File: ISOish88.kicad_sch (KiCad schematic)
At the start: 285 parts, among them J1 Conn_01x04_Pin, J3 USB_C_Receptacle_USB2.0_14P, K1 Esc, K10 F9, K11 F10, K12 F11, K13 F12, K14 Print, K15 Scroll, K16 Pause, K17 ` ~, K18 1, K19 2, K2 F1, K20 3, K21 4, K22 5, K23 6, K24 7, K25 8, K26 9, K27 0, K28 - _, K29 = +, K3 F2, K30 Backspace, K31 Ins, K32 Home, K33 PgUp, K34 Tab, K35 Q, K36 W, K37 E, K38 R, K39 T, K4 F3, K40 Y, K41 U, K42 I, K43 O, K44 P, K45 [ {, K46 ] }, K47 Enter, K48 Del, K49 End, K5 F4, K50 PgDn, K51 Caps, K52 A, K53 S, K54 D, K55 F, K56 G, K57 H, K58 J, K59 K, K6 F5, K60 L, K61 ; :, K62 ' ", K63 \ |, K64 LShift, K65 Z, K66 X, K67 C, K68 V, K69 B, K7 F6, K70 N, K71 M, K72 , <, K73 . >, K74 / ?, K75 SplitRShift, K76 Fn, K77 Up, K78 LCtrl, K79 LSys, K8 F7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

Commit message: initial f13 revision
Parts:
- added D47: 1N4148W, Diode_SMD:D_SOD-123, symbol Diode:1N4148W
- added K91: F13, Switch_Keyboard_Hotswap_Kailh_mine:SW_Hotswap_Kailh_MX_1.00u, symbol keyboard_parts:KEYSW
- added LD89: SK6812MINI-E, schizobovine:LED_SK6812MINI_PLCC4_3.1x2.7mm_P1.75mm_reverse_mount, symbol schizobovine:SK6812MINI
- BD1, BD10, BD11, BD12, BD13, BD14, BD15, BD16, BD2, BD3, BD4, BD5, BD6, BD7, BD8, BD9: footprint schizobovine:LED_WS2812B_NANO_2020 -> LED_SMD:LED_SK6812MINI_PLCC4_3.5x3.5mm_P1.75mm; symbol schizobovine:WS2812B -> schizobovine:SK6812MINI
- LD1, LD10, LD11, LD12, LD13, LD14, LD15, LD16, LD17, LD18, LD19, LD2, LD20, LD21, LD22, LD23, LD24, LD25, LD26, LD27, LD28, LD29, LD3, LD30, LD31, LD32, LD33, LD34, LD35, LD36, LD37, LD38, LD39, LD4, LD40, LD41, LD42, LD43, LD44, LD45, LD46, LD47, LD48, LD49, LD5, LD50, LD51, LD52, LD53, LD54, LD55, LD56, LD57, LD58, LD59, LD6, LD60, LD61, LD62, LD63, LD64, LD65, LD66, LD67, LD68, LD69, LD7, LD70, LD71, LD72, LD73, LD74, LD75, LD76, LD77, LD78, LD79, LD8, LD80, LD81, LD82, LD83, LD84, LD85, LD86, LD87, LD88, LD9: value WS2812B -> SK6812MINI-E; symbol schizobovine:WS2812B -> schizobovine:SK6812MINI
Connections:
- net +5V: now also BD1.1 (VDD), BD10.1 (VDD), BD11.1 (VDD), BD12.1 (VDD), BD13.1 (VDD), BD14.1 (VDD), BD15.1 (VDD), BD16.1 (VDD), BD2.1 (VDD), BD3.1 (VDD), BD4.1 (VDD), BD5.1 (VDD), BD6.1 (VDD), BD7.1 (VDD), BD8.1 (VDD), BD9.1 (VDD), LD1.1 (VDD), LD10.1 (VDD), LD11.1 (VDD), LD12.1 (VDD), LD13.1 (VDD), LD14.1 (VDD), LD15.1 (VDD), LD16.1 (VDD), LD17.1 (VDD), LD18.1 (VDD), LD19.1 (VDD), LD2.1 (VDD), LD20.1 (VDD), LD21.1 (VDD), LD22.1 (VDD), LD23.1 (VDD), LD24.1 (VDD), LD25.1 (VDD), LD26.1 (VDD), LD27.1 (VDD), LD28.1 (VDD), LD29.1 (VDD), LD3.1 (VDD), LD30.1 (VDD), LD31.1 (VDD), LD32.1 (VDD), LD33.1 (VDD), LD34.1 (VDD), LD35.1 (VDD), LD36.1 (VDD), LD37.1 (VDD), LD38.1 (VDD), LD39.1 (VDD), LD4.1 (VDD), LD40.1 (VDD), LD41.1 (VDD), LD42.1 (VDD), LD43.1 (VDD), LD44.1 (VDD), LD45.1 (VDD), LD46.1 (VDD), LD47.1 (VDD), LD48.1 (VDD), LD49.1 (VDD), LD5.1 (VDD), LD50.1 (VDD), LD51.1 (VDD), LD52.1 (VDD), LD53.1 (VDD), LD54.1 (VDD), LD55.1 (VDD), LD56.1 (VDD), LD57.1 (VDD), LD58.1 (VDD), LD59.1 (VDD), LD6.1 (VDD), LD60.1 (VDD), LD61.1 (VDD), LD62.1 (VDD), LD63.1 (VDD), LD64.1 (VDD), LD65.1 (VDD), LD66.1 (VDD), LD67.1 (VDD), LD68.1 (VDD), LD69.1 (VDD), LD7.1 (VDD), LD70.1 (VDD), LD71.1 (VDD), LD72.1 (VDD), LD73.1 (VDD), LD74.1 (VDD), LD75.1 (VDD), LD76.1 (VDD), LD77.1 (VDD), LD78.1 (VDD), LD79.1 (VDD), LD8.1 (VDD), LD80.1 (VDD), LD81.1 (VDD), LD82.1 (VDD), LD83.1 (VDD), LD84.1 (VDD), LD85.1 (VDD), LD86.1 (VDD), LD87.1 (VDD), LD88.1 (VDD), LD9.1 (VDD), LD89.1 (VDD); no longer BD1.4 (VDD), BD10.4 (VDD), BD11.4 (VDD), BD12.4 (VDD), BD13.4 (VDD), BD14.4 (VDD), BD15.4 (VDD), BD16.4 (VDD), BD2.4 (VDD), BD3.4 (VDD), BD4.4 (VDD), BD5.4 (VDD), BD6.4 (VDD), BD7.4 (VDD), BD8.4 (VDD), BD9.4 (VDD), LD1.4 (VDD), LD10.4 (VDD), LD11.4 (VDD), LD12.4 (VDD), LD13.4 (VDD), LD14.4 (VDD), LD15.4 (VDD), LD16.4 (VDD), LD17.4 (VDD), LD18.4 (VDD), LD19.4 (VDD), LD2.4 (VDD), LD20.4 (VDD), LD21.4 (VDD), LD22.4 (VDD), LD23.4 (VDD), LD24.4 (VDD), LD25.4 (VDD), LD26.4 (VDD), LD27.4 (VDD), LD28.4 (VDD), LD29.4 (VDD), LD3.4 (VDD), LD30.4 (VDD), LD31.4 (VDD), LD32.4 (VDD), LD33.4 (VDD), LD34.4 (VDD), LD35.4 (VDD), LD36.4 (VDD), LD37.4 (VDD), LD38.4 (VDD), LD39.4 (VDD), LD4.4 (VDD), LD40.4 (VDD), LD41.4 (VDD), LD42.4 (VDD), LD43.4 (VDD), LD44.4 (VDD), LD45.4 (VDD), LD46.4 (VDD), LD47.4 (VDD), LD48.4 (VDD), LD49.4 (VDD), LD5.4 (VDD), LD50.4 (VDD), LD51.4 (VDD), LD52.4 (VDD), LD53.4 (VDD), LD54.4 (VDD), LD55.4 (VDD), LD56.4 (VDD), LD57.4 (VDD), LD58.4 (VDD), LD59.4 (VDD), LD6.4 (VDD), LD60.4 (VDD), LD61.4 (VDD), LD62.4 (VDD), LD63.4 (VDD), LD64.4 (VDD), LD65.4 (VDD), LD66.4 (VDD), LD67.4 (VDD), LD68.4 (VDD), LD69.4 (VDD), LD7.4 (VDD), LD70.4 (VDD), LD71.4 (VDD), LD72.4 (VDD), LD73.4 (VDD), LD74.4 (VDD), LD75.4 (VDD), LD76.4 (VDD), LD77.4 (VDD), LD78.4 (VDD), LD79.4 (VDD), LD8.4 (VDD), LD80.4 (VDD), LD81.4 (VDD), LD82.4 (VDD), LD83.4 (VDD), LD84.4 (VDD), LD85.4 (VDD), LD86.4 (VDD), LD87.4 (VDD), LD88.4 (VDD), LD9.4 (VDD)
- net GND: now also BD1.3 (VSS), BD10.3 (VSS), BD11.3 (VSS), BD12.3 (VSS), BD13.3 (VSS), BD14.3 (VSS), BD15.3 (VSS), BD16.3 (VSS), BD2.3 (VSS), BD3.3 (VSS), BD4.3 (VSS), BD5.3 (VSS), BD6.3 (VSS), BD7.3 (VSS), BD8.3 (VSS), BD9.3 (VSS), LD1.3 (VSS), LD10.3 (VSS), LD11.3 (VSS), LD12.3 (VSS), LD13.3 (VSS), LD14.3 (VSS), LD15.3 (VSS), LD16.3 (VSS), LD17.3 (VSS), LD18.3 (VSS), LD19.3 (VSS), LD2.3 (VSS), LD20.3 (VSS), LD21.3 (VSS), LD22.3 (VSS), LD23.3 (VSS), LD24.3 (VSS), LD25.3 (VSS), LD26.3 (VSS), LD27.3 (VSS), LD28.3 (VSS), LD29.3 (VSS), LD3.3 (VSS), LD30.3 (VSS), LD31.3 (VSS), LD32.3 (VSS), LD33.3 (VSS), LD34.3 (VSS), LD35.3 (VSS), LD36.3 (VSS), LD37.3 (VSS), LD38.3 (VSS), LD39.3 (VSS), LD4.3 (VSS), LD40.3 (VSS), LD41.3 (VSS), LD42.3 (VSS), LD43.3 (VSS), LD44.3 (VSS), LD45.3 (VSS), LD46.3 (VSS), LD47.3 (VSS), LD48.3 (VSS), LD49.3 (VSS), LD5.3 (VSS), LD50.3 (VSS), LD51.3 (VSS), LD52.3 (VSS), LD53.3 (VSS), LD54.3 (VSS), LD55.3 (VSS), LD56.3 (VSS), LD57.3 (VSS), LD58.3 (VSS), LD59.3 (VSS), LD6.3 (VSS), LD60.3 (VSS), LD61.3 (VSS), LD62.3 (VSS), LD63.3 (VSS), LD64.3 (VSS), LD65.3 (VSS), LD66.3 (VSS), LD67.3 (VSS), LD68.3 (VSS), LD69.3 (VSS), LD7.3 (VSS), LD70.3 (VSS), LD71.3 (VSS), LD72.3 (VSS), LD73.3 (VSS), LD74.3 (VSS), LD75.3 (VSS), LD76.3 (VSS), LD77.3 (VSS), LD78.3 (VSS), LD79.3 (VSS), LD8.3 (VSS), LD80.3 (VSS), LD81.3 (VSS), LD82.3 (VSS), LD83.3 (VSS), LD84.3 (VSS), LD85.3 (VSS), LD86.3 (VSS), LD87.3 (VSS), LD88.3 (VSS), LD9.3 (VSS), LD89.3 (VSS); no longer BD1.2 (VSS), BD10.2 (VSS), BD11.2 (VSS), BD12.2 (VSS), BD13.2 (VSS), BD14.2 (VSS), BD15.2 (VSS), BD16.2 (VSS), BD2.2 (VSS), BD3.2 (VSS), BD4.2 (VSS), BD5.2 (VSS), BD6.2 (VSS), BD7.2 (VSS), BD8.2 (VSS), BD9.2 (VSS), LD1.2 (VSS), LD10.2 (VSS), LD11.2 (VSS), LD12.2 (VSS), LD13.2 (VSS), LD14.2 (VSS), LD15.2 (VSS), LD16.2 (VSS), LD17.2 (VSS), LD18.2 (VSS), LD19.2 (VSS), LD2.2 (VSS), LD20.2 (VSS), LD21.2 (VSS), LD22.2 (VSS), LD23.2 (VSS), LD24.2 (VSS), LD25.2 (VSS), LD26.2 (VSS), LD27.2 (VSS), LD28.2 (VSS), LD29.2 (VSS), LD3.2 (VSS), LD30.2 (VSS), LD31.2 (VSS), LD32.2 (VSS), LD33.2 (VSS), LD34.2 (VSS), LD35.2 (VSS), LD36.2 (VSS), LD37.2 (VSS), LD38.2 (VSS), LD39.2 (VSS), LD4.2 (VSS), LD40.2 (VSS), LD41.2 (VSS), LD42.2 (VSS), LD43.2 (VSS), LD44.2 (VSS), LD45.2 (VSS), LD46.2 (VSS), LD47.2 (VSS), LD48.2 (VSS), LD49.2 (VSS), LD5.2 (VSS), LD50.2 (VSS), LD51.2 (VSS), LD52.2 (VSS), LD53.2 (VSS), LD54.2 (VSS), LD55.2 (VSS), LD56.2 (VSS), LD57.2 (VSS), LD58.2 (VSS), LD59.2 (VSS), LD6.2 (VSS), LD60.2 (VSS), LD61.2 (VSS), LD62.2 (VSS), LD63.2 (VSS), LD64.2 (VSS), LD65.2 (VSS), LD66.2 (VSS), LD67.2 (VSS), LD68.2 (VSS), LD69.2 (VSS), LD7.2 (VSS), LD70.2 (VSS), LD71.2 (VSS), LD72.2 (VSS), LD73.2 (VSS), LD74.2 (VSS), LD75.2 (VSS), LD76.2 (VSS), LD77.2 (VSS), LD78.2 (VSS), LD79.2 (VSS), LD8.2 (VSS), LD80.2 (VSS), LD81.2 (VSS), LD82.2 (VSS), LD83.2 (VSS), LD84.2 (VSS), LD85.2 (VSS), LD86.2 (VSS), LD87.2 (VSS), LD88.2 (VSS), LD9.2 (VSS)
- net col1: now also K2.1
- net col10: now also K11.1; no longer K10.1
- net col11: now also K12.1; no longer K11.1
- net col12: now also K13.1; no longer K12.1
- net col13: now also K91.1; no longer K13.1
- net col2: now also K3.1; no longer K2.1
- net col3: now also K4.1; no longer K3.1
- net col4: now also K5.1; no longer K4.1
- net col5: now also K6.1; no longer K5.1
- net col6: now also K7.1; no longer K6.1
- net col7: now also K8.1; no longer K7.1
- net col8: now also K9.1; no longer K8.1
- net col9: now also K10.1; no longer K9.1
- net row0: now also D47.1 (K)
- net at D8.3 (K): now also K15.2; no longer K16.2
- net at D8.1 (A): now also K14.2; no longer K15.2
- net at JP1.1 (A): now also LD1.4 (DIN); no longer LD1.3 (DIN)
- net at D7.3 (K): now also K91.2; no longer K14.2
- new net: BD7.4 (DIN), BD8.2 (DOUT)
- new net: BD8.4 (DIN), BD9.2 (DOUT)
- new net: LD80.4 (DIN), LD81.2 (DOUT)
- new net: LD81.4 (DIN), LD82.2 (DOUT)
- new net: LD75.2 (DOUT), LD88.4 (DIN)
- new net: LD74.2 (DOUT), LD75.4 (DIN)
- new net: LD26.4 (DIN), LD27.2 (DOUT)
- new net: LD27.4 (DIN), LD28.2 (DOUT)
- new net: LD35.2 (DOUT), LD36.4 (DIN)
- new net: LD34.2 (DOUT), LD35.4 (DIN)
- new net: LD86.4 (DIN), LD87.2 (DOUT)
- new net: LD77.2 (DOUT), LD87.4 (DIN)
- new net: LD72.2 (DOUT), LD73.4 (DIN)
- new net: LD71.2 (DOUT), LD72.4 (DIN)
- new net: BD1.2 (DOUT), JP1.3 (B), LD78.2 (DOUT)
- new net: BD1.4 (DIN), BD2.2 (DOUT)
- new net: LD37.2 (DOUT), LD38.4 (DIN)
- new net: LD36.2 (DOUT), LD37.4 (DIN)
- new net: LD62.4 (DIN), LD63.2 (DOUT)
- new net: LD50.2 (DOUT), LD63.4 (DIN)
- new net: BD2.4 (DIN), BD3.2 (DOUT)
- new net: BD3.4 (DIN), BD4.2 (DOUT)
- new net: LD84.4 (DIN), LD85.2 (DOUT)
- new net: LD85.4 (DIN), LD86.2 (DOUT)
- new net: LD78.4 (DIN), LD79.2 (DOUT)
- new net: LD22.4 (DIN), LD23.2 (DOUT)
- new net: LD23.4 (DIN), LD24.2 (DOUT)
- new net: LD48.2 (DOUT), LD49.4 (DIN)
- new net: LD47.2 (DOUT), LD48.4 (DIN)
- new net: LD1.2 (DOUT), LD2.4 (DIN)
- new net: BD4.4 (DIN), BD5.2 (DOUT)
- new net: LD65.2 (DOUT), LD66.4 (DIN)
- new net: LD64.2 (DOUT), LD65.4 (DIN)
- new net: LD51.2 (DOUT), LD64.4 (DIN)
- new net: LD51.4 (DIN), LD52.2 (DOUT)
- new net: LD7.2 (DOUT), LD8.4 (DIN)
- new net: LD6.2 (DOUT), LD7.4 (DIN)
- new net: LD24.4 (DIN), LD25.2 (DOUT)
- new net: LD52.4 (DIN), LD53.2 (DOUT)
- new net: LD53.4 (DIN), LD54.2 (DOUT)
- new net: LD54.4 (DIN), LD55.2 (DOUT)
- new net: LD55.4 (DIN), LD56.2 (DOUT)
- new net: LD43.2 (DOUT), LD44.4 (DIN)
- new net: LD42.2 (DOUT), LD43.4 (DIN)
- new net: LD31.4 (DIN), LD32.2 (DOUT)
- new net: LD32.4 (DIN), LD33.2 (DOUT)
- new net: LD10.4 (DIN), LD9.2 (DOUT)
- new net: LD8.2 (DOUT), LD9.4 (DIN)
- new net: BD15.4 (DIN), BD16.2 (DOUT)
- new net: LD16.2 (DOUT), LD33.4 (DIN)
- new net: LD15.2 (DOUT), LD16.4 (DIN)
- new net: LD76.2 (DOUT), LD77.4 (DIN)
- new net: LD76.4 (DIN), LD88.2 (DOUT)
- new net: LD14.4 (DIN), LD89.2 (DOUT)
- new net: LD13.2 (DOUT), LD89.4 (DIN)
- new net: LD17.4 (DIN), LD18.2 (DOUT)
- new net: LD18.4 (DIN), LD19.2 (DOUT)
- new net: BD10.4 (DIN), BD11.2 (DOUT)
- new net: BD11.4 (DIN), BD12.2 (DOUT)
- new net: LD67.2 (DOUT), LD68.4 (DIN)
- new net: LD66.2 (DOUT), LD67.4 (DIN)
- new net: LD25.4 (DIN), LD26.2 (DOUT)
- new net: LD5.2 (DOUT), LD6.4 (DIN)
- new net: LD4.2 (DOUT), LD5.4 (DIN)
- new net: BD12.4 (DIN), BD13.2 (DOUT)
- new net: BD13.4 (DIN), BD14.2 (DOUT)
- new net: LD79.4 (DIN), LD80.2 (DOUT)
- new net: LD17.2 (DOUT), LD34.4 (DIN)
- new net: LD20.4 (DIN), LD21.2 (DOUT)
- new net: LD21.4 (DIN), LD22.2 (DOUT)
- new net: LD46.2 (DOUT), LD47.4 (DIN)
- new net: LD41.2 (DOUT), LD42.4 (DIN)
- new net: LD40.2 (DOUT), LD41.4 (DIN)
- new net: LD29.4 (DIN), LD30.2 (DOUT)
- new net: LD30.4 (DIN), LD31.2 (DOUT)
- new net: LD68.2 (DOUT), LD69.4 (DIN)
- new net: LD3.2 (DOUT), LD4.4 (DIN)
- new net: LD2.2 (DOUT), LD3.4 (DIN)
- new net: LD69.2 (DOUT), LD70.4 (DIN)
- new net: LD82.4 (DIN), LD83.2 (DOUT)
- new net: LD83.4 (DIN), LD84.2 (DOUT)
- new net: D47.2 (A), K16.2
- new net: BD14.4 (DIN), BD15.2 (DOUT)
- new net: LD44.2 (DOUT), LD45.4 (DIN)
- new net: LD19.4 (DIN), LD20.2 (DOUT)
- new net: BD6.4 (DIN), BD7.2 (DOUT)
- new net: LD45.2 (DOUT), LD46.4 (DIN)
- new net: LD73.2 (DOUT), LD74.4 (DIN)
- new net: LD38.2 (DOUT), LD39.4 (DIN)
- new net: LD61.4 (DIN), LD62.2 (DOUT)
- new net: LD56.4 (DIN), LD57.2 (DOUT)
- new net: LD49.2 (DOUT), LD50.4 (DIN)
- new net: LD11.2 (DOUT), LD12.4 (DIN)
- new net: LD10.2 (DOUT), LD11.4 (DIN)
- new net: LD39.2 (DOUT), LD40.4 (DIN)
- new net: LD59.4 (DIN), LD60.2 (DOUT)
- new net: LD60.4 (DIN), LD61.2 (DOUT)
- new net: LD70.2 (DOUT), LD71.4 (DIN)
- new net: LD57.4 (DIN), LD58.2 (DOUT)
- new net: LD58.4 (DIN), LD59.2 (DOUT)
- new net: LD14.2 (DOUT), LD15.4 (DIN)
- new net: LD28.4 (DIN), LD29.2 (DOUT)
- new net: LD12.2 (DOUT), LD13.4 (DIN)
- new net: BD10.2 (DOUT), BD9.4 (DIN)
- new net: BD5.4 (DIN), BD6.2 (DOUT)
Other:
- moved on the sheet: D1B, D2A, D2B, D3A, D3B, D4A, D4B, D5A, D5B, D6A, D6B, D7A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

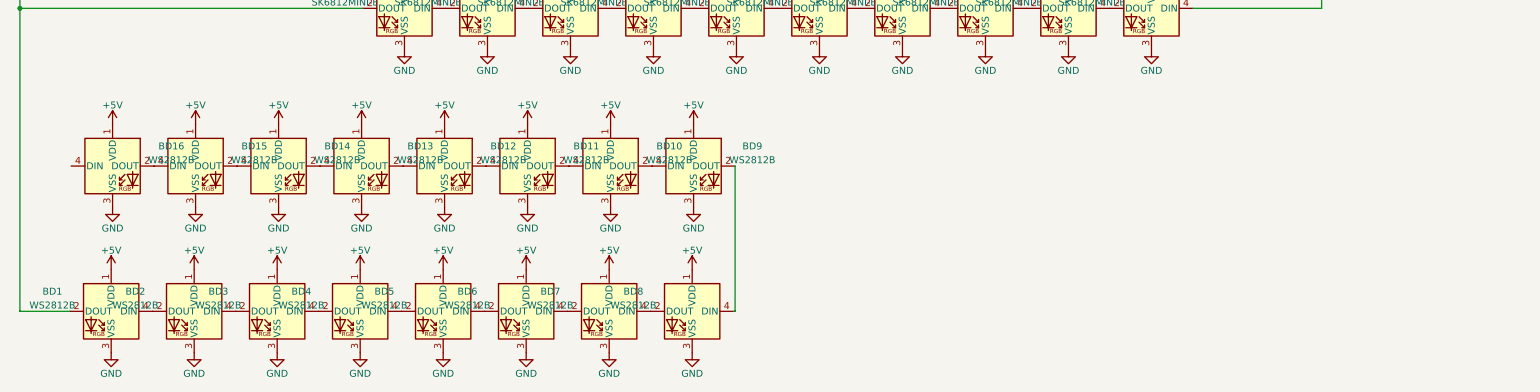
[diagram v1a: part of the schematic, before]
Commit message: more RGB footprint fixes
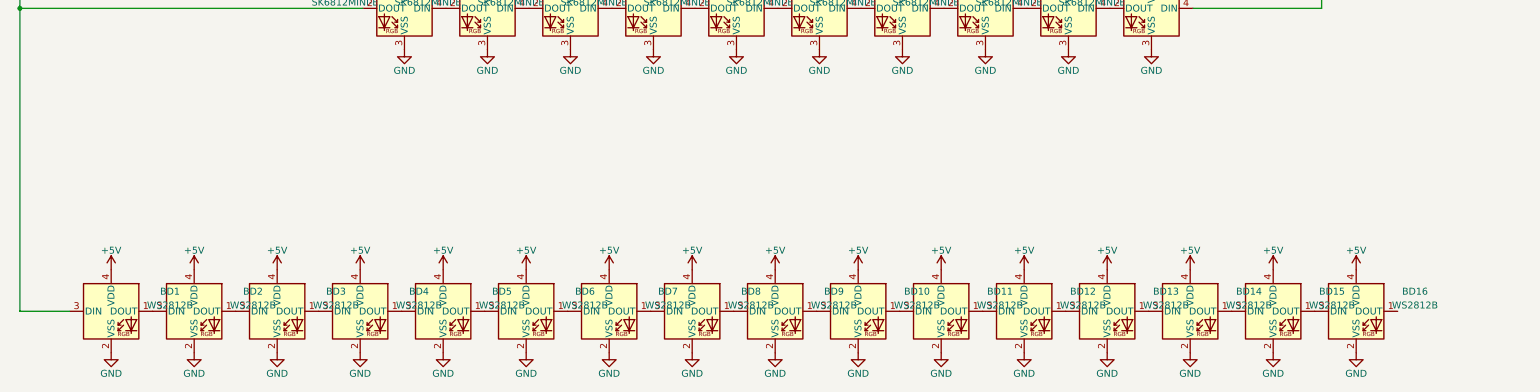
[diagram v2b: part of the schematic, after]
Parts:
- BD1, BD10, BD11, BD12, BD13, BD14, BD15, BD16, BD2, BD3, BD4, BD5, BD6, BD7, BD8, BD9: symbol schizobovine:SK6812MINI -> LED:SK6805
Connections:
- net +5V: now also BD1.4 (VDD), BD10.4 (VDD), BD11.4 (VDD), BD12.4 (VDD), BD13.4 (VDD), BD14.4 (VDD), BD15.4 (VDD), BD16.4 (VDD), BD2.4 (VDD), BD3.4 (VDD), BD4.4 (VDD), BD5.4 (VDD), BD6.4 (VDD), BD7.4 (VDD), BD8.4 (VDD), BD9.4 (VDD); no longer BD1.1 (VDD), BD10.1 (VDD), BD11.1 (VDD), BD12.1 (VDD), BD13.1 (VDD), BD14.1 (VDD), BD15.1 (VDD), BD16.1 (VDD), BD2.1 (VDD), BD3.1 (VDD), BD4.1 (VDD), BD5.1 (VDD), BD6.1 (VDD), BD7.1 (VDD), BD8.1 (VDD), BD9.1 (VDD)
- net GND: now also BD1.2 (VSS), BD10.2 (VSS), BD11.2 (VSS), BD12.2 (VSS), BD13.2 (VSS), BD14.2 (VSS), BD15.2 (VSS), BD16.2 (VSS), BD2.2 (VSS), BD3.2 (VSS), BD4.2 (VSS), BD5.2 (VSS), BD6.2 (VSS), BD7.2 (VSS), BD8.2 (VSS), BD9.2 (VSS); no longer BD1.3 (VSS), BD10.3 (VSS), BD11.3 (VSS), BD12.3 (VSS), BD13.3 (VSS), BD14.3 (VSS), BD15.3 (VSS), BD16.3 (VSS), BD2.3 (VSS), BD3.3 (VSS), BD4.3 (VSS), BD5.3 (VSS), BD6.3 (VSS), BD7.3 (VSS), BD8.3 (VSS), BD9.3 (VSS)
- net at JP1.3 (B), LD78.2 (DOUT): now also BD1.3 (DIN); no longer BD1.2 (DOUT)
- new net: BD8.1 (DOUT), BD9.3 (DIN)
- new net: BD7.1 (DOUT), BD8.3 (DIN)
- new net: BD1.1 (DOUT), BD2.3 (DIN)
- new net: BD3.1 (DOUT), BD4.3 (DIN)
- new net: BD2.1 (DOUT), BD3.3 (DIN)
- new net: BD4.1 (DOUT), BD5.3 (DIN)
- new net: BD15.1 (DOUT), BD16.3 (DIN)
- new net: BD11.1 (DOUT), BD12.3 (DIN)
- new net: BD10.1 (DOUT), BD11.3 (DIN)
- new net: BD13.1 (DOUT), BD14.3 (DIN)
- new net: BD12.1 (DOUT), BD13.3 (DIN)
- new net: BD14.1 (DOUT), BD15.3 (DIN)
- new net: BD6.1 (DOUT), BD7.3 (DIN)
- new net: BD10.3 (DIN), BD9.1 (DOUT)
- new net: BD5.1 (DOUT), BD6.3 (DIN)
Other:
- moved on the sheet: BD10, BD11, BD12, BD13, BD14, BD15, BD16, BD9

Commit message: tweaks
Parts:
- added C10, C17, C18, C7, C8: 1u, schizobovine:C_0603_1608Metric, symbol Device:C_Small
- C12: value 1u -> 4u7; footprint schizobovine:C_0603_1608Metric -> schizobovine:C_0805_2012Metric
- H1, H2, H3, H4: footprint schizobovine:MountingHole_2.2mm_M2_Pad_TopOnly -> schizobovine:MountingHole_3.0mm_M2_5mm_dia_solderable
- U5: footprint MCU_RaspberryPi_and_Boards:RP2040-QFN-56 -> schizobovine:RP2040-QFN-56
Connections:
- net +5V: now also C10.1, C17.1, C18.1, C7.1, C8.1
- net GND: now also C10.2, C17.2, C18.2, C7.2, C8.2
